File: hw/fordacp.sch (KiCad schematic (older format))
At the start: 26 parts, among them P1 CONN_02X06

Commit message: pcb first try
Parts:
- added C10, C11: 2u2/10V, Capacitors_SMD:c_elec_5x5.3, symbol CP
- added D1: GREEN, LEDs:LED-1206, symbol LED
- added D2: RED, LEDs:LED-1206, symbol LED
- added R4, R5: 470, Resistors_SMD:R_0805_HandSoldering, symbol R
- added R8, R9: 4k7, Resistors_SMD:R_0805_HandSoldering, symbol R
- added programing1: CONN_01X02, Pin_Headers:Pin_Header_Straight_1x02, symbol CONN_01X04
- C1: renamed from C?; footprint (none) -> Capacitors_Tantalum_SMD:TantalC_SizeD_EIA-7343_HandSoldering
- C2, C5, C6, C7, C8, C9: renamed from C?; footprint (none) -> Capacitors_SMD:C_1206_HandSoldering
- C3: renamed from C?; footprint (none) -> Capacitors_SMD:c_elec_4x5.3
- C4: renamed from C?; footprint (none) -> Capacitors_SMD:c_elec_5x5.3
- D3: renamed from D?; footprint (none) -> Diodes_SMD:MiniMELF_Standard
- IC1: renamed from IC?; footprint TQFP100 -> Housings_QFP:TQFP-100_14x14mm_Pitch0.5mm
- L1: renamed from L?; footprint (none) -> SMD_Packages:SMD-1206_Pol
- MIC1: renamed from MIC; footprint (none) -> Pin_Headers:Pin_Header_Straight_1x02
- R1, R2, R3, R6, R7: renamed from R?; footprint (none) -> Resistors_SMD:R_0805_HandSoldering
- RV1: renamed from RV?; value POT -> 1k; footprint (none) -> Potentiometers:Potentiometer_Bourns_3339H_Angular_ScrewUp
- U2: renamed from U?; footprint (none) -> my_modules:SOT-223-REGULATOR; symbol AP1117D50 -> 78L05
- Y1: renamed from Y?; footprint (none) -> Crystals_Oscillators_SMD:Q_49U3HMS
- gave numbers to parts that had none: 4
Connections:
- wire segments 158 -> 184
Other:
- moved on the sheet: C5, C6, C7, C8, MIC1, U1

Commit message: change modules to 1206 for 1u 2u2 4u7 capacitors
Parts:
- C10, C11: footprint Capacitors_SMD:c_elec_5x5.3 -> Capacitors_SMD:C_0805_HandSoldering; symbol CP -> C
- C2, C5, C6, C7, C8, C9: footprint Capacitors_SMD:C_1206_HandSoldering -> Capacitors_SMD:C_0805_HandSoldering
- C3: footprint Capacitors_SMD:c_elec_4x5.3 -> Capacitors_SMD:C_0805_HandSoldering; symbol CP -> C
- C4: footprint Capacitors_SMD:c_elec_5x5.3 -> Capacitors_SMD:C_1206_HandSoldering; symbol CP -> C
- programing1: footprint Pin_Headers:Pin_Header_Straight_1x02 -> Pin_Headers:Pin_Header_Straight_1x04

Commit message: update
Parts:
- C10, C11: value 2u2/10V -> 1u/16V
- R1: value 2k7 -> 2k7(3k3)
- R8, R9: value 4k7 -> 10k
- programing1: value CONN_01X02 -> CONN_01X05; footprint Pin_Headers:Pin_Header_Straight_1x04 -> Pin_Headers:Pin_Header_Straight_1x05; symbol CONN_01X04 -> CONN_01X05
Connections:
- net +5V: now also programing1.4 (P4); no longer programing1.3 (P3)
- net ARD_RESET: now also programing1.1 (P1)
- net GND: now also programing1.5 (P5); no longer programing1.4 (P4)
- net RX0: now also programing1.2 (P2); no longer programing1.1 (P1)
- net TX0: now also programing1.3 (P3); no longer programing1.2 (P2)
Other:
- moved on the sheet: C9, D1, D2, R4, R5
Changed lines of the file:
@@
 P 2550 3400
 F 0 "R1" V 2630 3400 50  0000 C CNN
-F 1 "2k7" V 2550 3400 50  0000 C CNN
+F 1 "2k7(3k3)" V 2550 3400 50  0000 C CNN
 F 2 "Resistors_SMD:R_0805_HandSoldering" V 2250 3350 30  0001 C CNN
 F 3 "" H 2550 3400 30  0000 C CNN
@@
 	1    0    0    -1
 $EndComp
-Text Label 8050 5700 0    60   ~ 0
+Text Label 8050 5800 0    60   ~ 0
 ARD_AREF
 $Comp
 L C C9
 U 1 1 561F7DDA
-P 8550 6000
-F 0 "C9" H 8575 6100 50  0000 L CNN
-F 1 "100n/50V" H 8575 5900 50  0000 L CNN
-F 2 "Capacitors_SMD:C_0805_HandSoldering" H 8588 5850 30  0001 C CNN
-F 3 "" H 8550 6000 60  0000 C CNN
-	1    8550 6000
+P 8550 6100
+F 0 "C9" H 8575 6200 50  0000 L CNN
+F 1 "100n/50V" H 8575 6000 50  0000 L CNN
+F 2 "Capacitors_SMD:C_0805_HandSoldering" H 8588 5950 30  0001 C CNN
+F 3 "" H 8550 6100 60  0000 C CNN
+	1    8550 6100
 	1    0    0    -1
 $EndComp
@@
 L GND #PWR021
 U 1 1 561F7E59
-P 8550 6250
-F 0 "#PWR021" H 8550 6000 50  0001 C CNN
-F 1 "GND" H 8550 6100 50  0000 C CNN
-F 2 "" H 8550 6250 60  0000 C CNN
-F 3 "" H 8550 6250 60  0000 C CNN
-	1    8550 6250
+P 8550 6350
+F 0 "#PWR021" H 8550 6100 50  0001 C CNN
+F 1 "GND" H 8550 6200 50  0000 C CNN
+F 2 "" H 8550 6350 60  0000 C CNN
+F 3 "" H 8550 6350 60  0000 C CNN
+	1    8550 6350
 	1    0    0    -1
 $EndComp
@@
 Text Label 3150 5450 0    60   ~ 0
 BT_WAKE
-Text Label 8800 4400 2    60   ~ 0
+Text Label 8800 4350 2    60   ~ 0
 BT_RX
-Text Label 8800 4500 2    60   ~ 0
+Text Label 8800 4450 2    60   ~ 0
 BT_TX
-Text Label 7450 4500 0    60   ~ 0
+Text Label 7450 4450 0    60   ~ 0
 RX2
-Text Label 7450 4400 0    60   ~ 0
+Text Label 7450 4350 0    60   ~ 0
 TX2
 Text Label 800  4800 0    60   ~ 0
@@
 Text Label 800  5200 0    60   ~ 0
 RS485_DI
-Text Label 7450 4600 0    60   ~ 0
+Text Label 7450 4550 0    60   ~ 0
 RX1
-Text Label 7450 4700 0    60   ~ 0
+Text Label 7450 4650 0    60   ~ 0
 TX1
-Text Label 8800 4600 2    60   ~ 0
+Text Label 8800 4550 2    60   ~ 0
 RS485_R0
-Text Label 8800 4700 2    60   ~ 0
+Text Label 8800 4650 2    60   ~ 0
 RS485_DI
 Text Label 2700 5100 2    60   ~ 0
@@
 L LED D1
 U 1 1 56211C21
-P 8150 4150
-F 0 "D1" H 8350 4050 50  0000 C CNN
-F 1 "GREEN" H 8000 4050 50  0000 C CNN
-F 2 "LEDs:LED-1206" H 8150 3900 60  0001 C CNN
-F 3 "" H 8150 4150 60  0000 C CNN
-	1    8150 4150
+P 8150 4100
+F 0 "D1" H 8350 4000 50  0000 C CNN
+F 1 "GREEN" H 8000 4000 50  0000 C CNN
+F 2 "LEDs:LED-1206" H 8150 3850 60  0001 C CNN
+F 3 "" H 8150 4100 60  0000 C CNN
+	1    8150 4100
 	-1   0    0    1
 $EndComp
@@
 L LED D2
 U 1 1 56211CB9
-P 8150 4250
-F 0 "D2" H 8350 4350 50  0000 C CNN
-F 1 "RED" H 8000 4350 50  0000 C CNN
-F 2 "LEDs:LED-1206" H 8150 3950 60  0001 C CNN
-F 3 "" H 8150 4250 60  0000 C CNN
-	1    8150 4250
+P 8150 4200
+F 0 "D2" H 8350 4300 50  0000 C CNN
+F 1 "RED" H 8000 4300 50  0000 C CNN
+F 2 "LEDs:LED-1206" H 8150 3900 60  0001 C CNN
+F 3 "" H 8150 4200 60  0000 C CNN
+	1    8150 4200
 	-1   0    0    1
 $EndComp
@@
 L +5V #PWR027
 U 1 1 5621209A
-P 7450 4050
-F 0 "#PWR027" H 7450 3900 50  0001 C CNN
-F 1 "+5V" H 7450 4190 50  0000 C CNN
-F 2 "" H 7450 4050 60  0000 C CNN
-F 3 "" H 7450 4050 60  0000 C CNN
-	1    7450 4050
-	1    0    0    -1
-$EndComp
-Text Label 8800 4150 2    60   ~ 0
+P 7450 4000
+F 0 "#PWR027" H 7450 3850 50  0001 C CNN
+F 1 "+5V" H 7450 4140 50  0000 C CNN
+F 2 "" H 7450 4000 60  0000 C CNN
+F 3 "" H 7450 4000 60  0000 C CNN
+	1    7450 4000
+	1    0    0    -1
+$EndComp
+Text Label 8800 4100 2    60   ~ 0
 LED1
-Text Label 8800 4250 2    60   ~ 0
+Text Label 8800 4200 2    60   ~ 0
 LED2
 $Comp
 L R R5
 U 1 1 562135C7
-P 7700 4250
-F 0 "R5" V 7600 4250 50  0000 C CNN
-F 1 "470" V 7700 4250 50  0000 C CNN
-F 2 "Resistors_SMD:R_0805_HandSoldering" V 8100 4250 30  0001 C CNN
-F 3 "" H 7700 4250 30  0000 C CNN
-	1    7700 4250
+P 7700 4200
+F 0 "R5" V 7600 4200 50  0000 C CNN
+F 1 "470" V 7700 4200 50  0000 C CNN
+F 2 "Resistors_SMD:R_0805_HandSoldering" V 8100 4200 30  0001 C CNN
+F 3 "" H 7700 4200 30  0000 C CNN
+	1    7700 4200
 	0    -1   -1   0
 $EndComp
@@
 L R R4
 U 1 1 56213872
-P 7700 4150
-F 0 "R4" V 7780 4150 50  0000 C CNN
-F 1 "470" V 7700 4150 50  0000 C CNN
-F 2 "Resistors_SMD:R_0805_HandSoldering" V 8050 4150 30  0001 C CNN
-F 3 "" H 7700 4150 30  0000 C CNN
-	1    7700 4150
+P 7700 4100
+F 0 "R4" V 7780 4100 50  0000 C CNN
+F 1 "470" V 7700 4100 50  0000 C CNN
+F 2 "Resistors_SMD:R_0805_HandSoldering" V 8050 4100 30  0001 C CNN
+F 3 "" H 7700 4100 30  0000 C CNN
+	1    7700 4100
 	0    -1   -1   0
 $EndComp
@@
 	1800 5400 1800 5600
 Wire Wire Line
-	8050 5700 8550 5700
-Wire Wire Line
-	8550 5700 8550 5850
-Wire Wire Line
-	8550 6250 8550 6150
+	8050 5800 8550 5800
+Wire Wire Line
+	8550 5800 8550 5950
+Wire Wire Line
+	8550 6350 8550 6250
 Wire Wire Line
 	5200 6850 5200 7100
@@
 	3750 5450 3150 5450
 Wire Wire Line
-	7450 4400 8800 4400
-Wire Wire Line
-	7450 4500 8800 4500
+	7450 4350 8800 4350
+Wire Wire Line
+	7450 4450 8800 4450
 Wire Wire Line
 	800  4800 1400 4800
@@
 	800  5200 1400 5200
 Wire Wire Line
-	7450 4600 8800 4600
-Wire Wire Line
-	7450 4700 8800 4700
+	7450 4550 8800 4550
+Wire Wire Line
+	7450 4650 8800 4650
 Wire Wire Line
 	2850 3200 2850 3400
@@
 	2850 3500 2850 3850
 Wire Wire Line
-	8350 4150 8800 4150
-Wire Wire Line
-	8800 4250 8350 4250
-Wire Wire Line
-	7450 4050 7450 4250
-Connection ~ 7450 4150
-Wire Wire Line
-	7450 4150 7550 4150
-Wire Wire Line
-	7450 4250 7550 4250
-Wire Wire Line
-	7850 4250 7950 4250
-Wire Wire Line
-	7850 4150 7950 4150
-$Comp
-L CONN_01X04 programing1
+	8350 4100 8800 4100
+Wire Wire Line
+	8800 4200 8350 4200
+Wire Wire Line
+	7450 4000 7450 4200
+Connection ~ 7450 4100
+Wire Wire Line
+	7450 4100 7550 4100
+Wire Wire Line
+	7450 4200 7550 4200
+Wire Wire Line
+	7850 4200 7950 4200
+Wire Wire Line
+	7850 4100 7950 4100
+$Comp
+L CONN_01X05 programing1
 U 1 1 562221CD
 P 8700 5150
 F 0 "programing1" H 8700 5300 50  0000 C CNN
-F 1 "CONN_01X02" V 8800 5150 50  0000 C CNN
-F 2 "Pin_Headers:Pin_Header_Straight_1x04" V 8900 5200 60  0001 C CNN
+F 1 "CONN_01X05" V 8800 5150 50  0000 C CNN
+F 2 "Pin_Headers:Pin_Header_Straight_1x05" V 8900 5200 60  0001 C CNN
 F 3 "" H 8700 5150 60  0000 C CNN
 	1    8700 5150
 	1    0    0    -1
 $EndComp
-Text Label 7450 5000 0    60   ~ 0
+Text Label 7450 5050 0    60   ~ 0
 RX0
-Text Label 7450 5100 0    60   ~ 0
+Text Label 7450 5150 0    60   ~ 0
 TX0
 Wire Wire Line
-	8500 5000 7450 5000
-Wire Wire Line
-	7450 5100 8500 5100
-Wire Wire Line
-	8250 5200 8500 5200
-Wire Wire Line
-	8250 5200 8250 4950
-Wire Wire Line
-	8500 5300 8250 5300
-Wire Wire Line
-	8250 5300 8250 5450
+	8500 5050 7450 5050
+Wire Wire Line
+	7450 5150 8500 5150
+Wire Wire Line
+	8250 5250 8500 5250
+Wire Wire Line
+	8250 4850 8250 5250
+Wire Wire Line
+	8500 5350 8250 5350
+Wire Wire Line
+	8250 5350 8250 5500
 $Comp
 L GND #PWR028
 U 1 1 56223162
-P 8250 5450
-F 0 "#PWR028" H 8250 5200 50  0001 C CNN
-F 1 "GND" H 8250 5300 50  0000 C CNN
-F 2 "" H 8250 5450 60  0000 C CNN
-F 3 "" H 8250 5450 60  0000 C CNN
-	1    8250 5450
+P 8250 5500
+F 0 "#PWR028" H 8250 5250 50  0001 C CNN
+F 1 "GND" H 8250 5350 50  0000 C CNN
+F 2 "" H 8250 5500 60  0000 C CNN
+F 3 "" H 8250 5500 60  0000 C CNN
+	1    8250 5500
 	1    0    0    -1
 $EndComp
@@
 L +5V #PWR029
 U 1 1 562285BA
-P 8250 4950
-F 0 "#PWR029" H 8250 4800 50  0001 C CNN
-F 1 "+5V" H 8250 5090 50  0000 C CNN
-F 2 "" H 8250 4950 60  0000 C CNN
-F 3 "" H 8250 4950 60  0000 C CNN
-	1    8250 4950
+P 8250 4850
+F 0 "#PWR029" H 8250 4700 50  0001 C CNN
+F 1 "+5V" H 8250 4990 50  0000 C CNN
+F 2 "" H 8250 4850 60  0000 C CNN
+F 3 "" H 8250 4850 60  0000 C CNN
+	1    8250 4850
 	1    0    0    -1
 $EndComp
@@
 P 7750 2700
 F 0 "R9" V 7830 2700 50  0000 C CNN
-F 1 "4k7" V 7750 2700 50  0000 C CNN
+F 1 "10k" V 7750 2700 50  0000 C CNN
 F 2 "Resistors_SMD:R_0805_HandSoldering" V 8100 2700 30  0001 C CNN
 F 3 "" H 7750 2700 30  0000 C CNN
@@
 P 7500 2950
 F 0 "C11" H 7525 3050 50  0000 L CNN
-F 1 "2u2/10V" H 7525 2850 50  0000 L CNN
+F 1 "1u/16V" H 7525 2850 50  0000 L CNN
 F 2 "Capacitors_SMD:C_0805_HandSoldering" H 7150 2800 30  0001 C CNN
 F 3 "" H 7500 2950 60  0000 C CNN
@@
 P 7500 1300
 F 0 "R8" V 7580 1300 50  0000 C CNN
-F 1 "4k7" V 7500 1300 50  0000 C CNN
+F 1 "10k" V 7500 1300 50  0000 C CNN
 F 2 "Resistors_SMD:R_0805_HandSoldering" V 7850 1300 30  0001 C CNN
 F 3 "" H 7500 1300 30  0000 C CNN
@@
 P 7250 1550
 F 0 "C10" H 7275 1650 50  0000 L CNN
-F 1 "2u2/10V" H 7275 1450 50  0000 L CNN
+F 1 "1u/16V" H 7275 1450 50  0000 L CNN
 F 2 "Capacitors_SMD:C_0805_HandSoldering" H 6900 1400 30  0001 C CNN
 F 3 "" H 7250 1550 60  0000 C CNN
@@
 Text Label 7550 1150 2    60   ~ 0
 ARD_RESET
+Wire Wire Line
+	8500 4950 7450 4950
+Text Label 7450 4950 0    60   ~ 0
+ARD_RESET
 $EndSCHEMATC

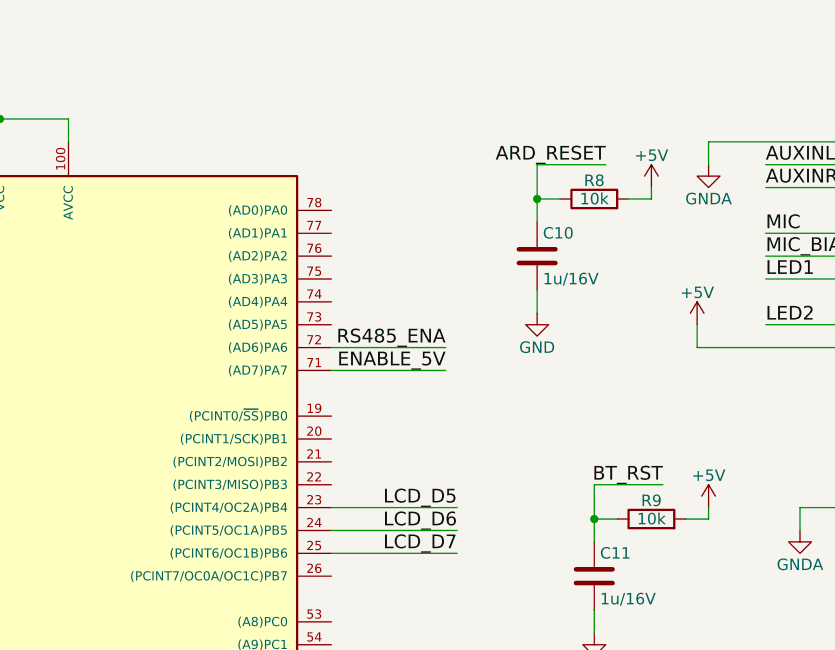
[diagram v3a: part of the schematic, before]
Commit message: added SPI interface
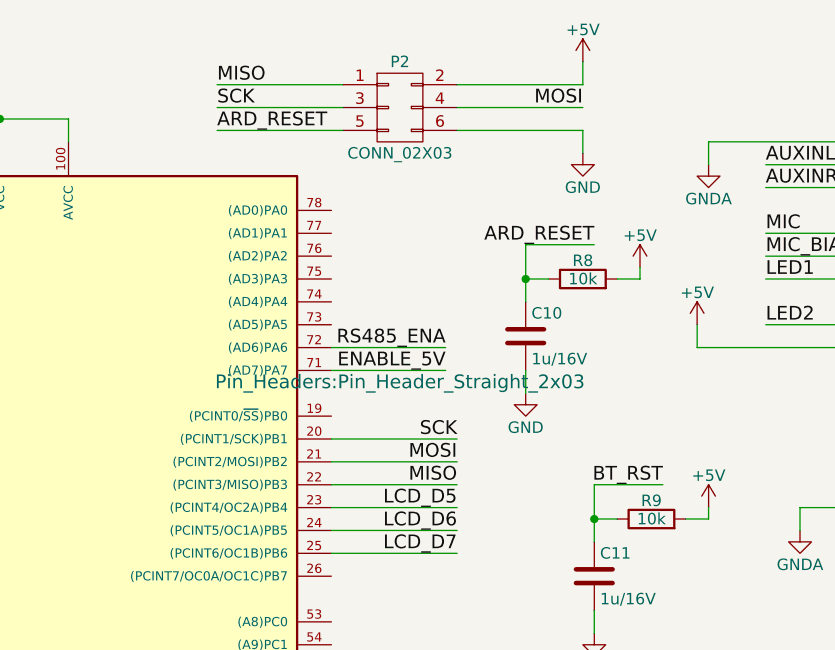
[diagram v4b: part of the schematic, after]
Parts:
- added P2: CONN_02X03, Pin_Headers:Pin_Header_Straight_2x03, symbol CONN_02X03
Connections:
- net +5V: now also P2.2 (P2)
- net ARD_RESET: now also P2.5 (P5)
- net GND: now also P2.6 (P6)
- net SCK: now reaches IC1.20 ((PCINT1/SCK)PB1)
- net SCK: now also P2.3 (P3)
- net MOSI: now reaches IC1.21 ((PCINT2/MOSI)PB2)
- net MOSI: now also P2.4 (P4)
- net MISO: now reaches IC1.22 ((PCINT3/MISO)PB3)
- net MISO: now also P2.1 (P1)
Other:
- moved on the sheet: C10, R8
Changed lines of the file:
@@
 	7500 3200 7500 3100
 Wire Wire Line
-	7550 1150 7250 1150
+	7500 1500 7200 1500
 Wire Wire Line
-	7250 1150 7250 1400
+	7200 1500 7200 1750
 $Comp
 L R R8
 U 1 1 5622B397
-P 7500 1300
-F 0 "R8" V 7580 1300 50  0000 C CNN
-F 1 "10k" V 7500 1300 50  0000 C CNN
-F 2 "Resistors_SMD:R_0805_HandSoldering" V 7850 1300 30  0001 C CNN
-F 3 "" H 7500 1300 30  0000 C CNN
-	1    7500 1300
+P 7450 1650
+F 0 "R8" V 7530 1650 50  0000 C CNN
+F 1 "10k" V 7450 1650 50  0000 C CNN
+F 2 "Resistors_SMD:R_0805_HandSoldering" V 7800 1650 30  0001 C CNN
+F 3 "" H 7450 1650 30  0000 C CNN
+	1    7450 1650
 	0    -1   -1   0
 $EndComp
@@
 L C C10
 U 1 1 5622B39D
-P 7250 1550
-F 0 "C10" H 7275 1650 50  0000 L CNN
-F 1 "1u/16V" H 7275 1450 50  0000 L CNN
-F 2 "Capacitors_SMD:C_0805_HandSoldering" H 6900 1400 30  0001 C CNN
-F 3 "" H 7250 1550 60  0000 C CNN
-	1    7250 1550
+P 7200 1900
+F 0 "C10" H 7225 2000 50  0000 L CNN
+F 1 "1u/16V" H 7225 1800 50  0000 L CNN
+F 2 "Capacitors_SMD:C_0805_HandSoldering" H 6850 1750 30  0001 C CNN
+F 3 "" H 7200 1900 60  0000 C CNN
+	1    7200 1900
 	1    0    0    -1
 $EndComp
 Wire Wire Line
-	7350 1300 7250 1300
-Connection ~ 7250 1300
+	7300 1650 7200 1650
+Connection ~ 7200 1650
 $Comp
 L GND #PWR032
 U 1 1 5622B3A5
-P 7250 1800
-F 0 "#PWR032" H 7250 1550 50  0001 C CNN
-F 1 "GND" H 7250 1650 50  0000 C CNN
-F 2 "" H 7250 1800 60  0000 C CNN
-F 3 "" H 7250 1800 60  0000 C CNN
-	1    7250 1800
+P 7200 2150
+F 0 "#PWR032" H 7200 1900 50  0001 C CNN
+F 1 "GND" H 7200 2000 50  0000 C CNN
+F 2 "" H 7200 2150 60  0000 C CNN
+F 3 "" H 7200 2150 60  0000 C CNN
+	1    7200 2150
 	1    0    0    -1
 $EndComp
@@
 L +5V #PWR033
 U 1 1 5622B3AB
-P 7750 1250
-F 0 "#PWR033" H 7750 1100 50  0001 C CNN
-F 1 "+5V" H 7750 1390 50  0000 C CNN
-F 2 "" H 7750 1250 60  0000 C CNN
-F 3 "" H 7750 1250 60  0000 C CNN
-	1    7750 1250
+P 7700 1600
+F 0 "#PWR033" H 7700 1450 50  0001 C CNN
+F 1 "+5V" H 7700 1740 50  0000 C CNN
+F 2 "" H 7700 1600 60  0000 C CNN
+F 3 "" H 7700 1600 60  0000 C CNN
+	1    7700 1600
 	1    0    0    -1
 $EndComp
 Wire Wire Line
-	7750 1250 7750 1300
+	7700 1600 7700 1650
 Wire Wire Line
-	7750 1300 7650 1300
+	7700 1650 7600 1650
 Wire Wire Line
-	7250 1800 7250 1700
-Text Label 7550 1150 2    60   ~ 0
+	7200 2150 7200 2050
+Text Label 7500 1500 2    60   ~ 0
 ARD_RESET
 Wire Wire Line
@@
 Text Label 7450 4950 0    60   ~ 0
 ARD_RESET
+$Comp
+L CONN_02X03 P2
+U 1 1 564ED864
+P 6650 900
+F 0 "P2" H 6650 1100 50  0000 C CNN
+F 1 "CONN_02X03" H 6650 700 50  0000 C CNN
+F 2 "Pin_Headers:Pin_Header_Straight_2x03" H 6650 -300 60  0000 C CNN
+F 3 "" H 6650 -300 60  0000 C CNN
+	1    6650 900
+	1    0    0    -1
+$EndComp
+Wire Wire Line
+	6900 800  7450 800
+Wire Wire Line
+	6900 900  7450 900
+Wire Wire Line
+	6900 1000 7450 1000
+Wire Wire Line
+	5850 800  6400 800
+Wire Wire Line
+	5850 900  6400 900
+Wire Wire Line
+	5850 1000 6400 1000
+Text Label 5850 1000 0    60   ~ 0
+ARD_RESET
+$Comp
+L +5V #PWR034
+U 1 1 564F125C
+P 7450 700
+F 0 "#PWR034" H 7450 550 50  0001 C CNN
+F 1 "+5V" H 7450 840 50  0000 C CNN
+F 2 "" H 7450 700 60  0000 C CNN
+F 3 "" H 7450 700 60  0000 C CNN
+	1    7450 700
+	1    0    0    -1
+$EndComp
+Wire Wire Line
+	7450 800  7450 700
+$Comp
+L GND #PWR035
+U 1 1 564F1C90
+P 7450 1100
+F 0 "#PWR035" H 7450 850 50  0001 C CNN
+F 1 "GND" H 7450 950 50  0000 C CNN
+F 2 "" H 7450 1100 60  0000 C CNN
+F 3 "" H 7450 1100 60  0000 C CNN
+	1    7450 1100
+	1    0    0    -1
+$EndComp
+Wire Wire Line
+	7450 1000 7450 1100
+Wire Wire Line
+	6900 2450 6350 2450
+Wire Wire Line
+	6900 2350 6350 2350
+Wire Wire Line
+	6350 2550 6900 2550
+Text Label 6900 2350 2    60   ~ 0
+SCK
+Text Label 6900 2450 2    60   ~ 0
+MOSI
+Text Label 6900 2550 2    60   ~ 0
+MISO
+Text Label 5850 900  0    60   ~ 0
+SCK
+Text Label 5850 800  0    60   ~ 0
+MISO
+Text Label 7450 900  2    60   ~ 0
+MOSI
 $EndSCHEMATC
